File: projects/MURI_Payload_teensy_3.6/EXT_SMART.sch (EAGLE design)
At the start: 5 parts, among them U1 XBEE

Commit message: Fixed my stupid shit.
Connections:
- net VDD renamed 5V
- net PWM: now also U$1.D4
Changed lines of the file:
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@@
 <wire x1="147.32" y1="25.4" x2="182.88" y2="25.4" width="0.1524" layer="91"/>
 <wire x1="182.88" y1="25.4" x2="182.88" y2="50.8" width="0.1524" layer="91"/>
+<label x="43.18" y="25.4" size="1.778" layer="95"/>
 </segment>
 </net>
-<net name="VDD" class="0">
+<net name="5V" class="0">
 <segment>
 <label x="147.32" y="63.5" size="1.778" layer="95"/>
@@
 <wire x1="180.34" y1="53.34" x2="180.34" y2="83.82" width="0.1524" layer="91"/>
 <wire x1="180.34" y1="83.82" x2="147.32" y2="83.82" width="0.1524" layer="91"/>
+<label x="43.18" y="83.82" size="1.778" layer="95"/>
 </segment>
 </net>
@@
 <label x="175.26" y="55.88" size="1.778" layer="95" rot="MR0" xref="yes"/>
 </segment>
+<segment>
+<pinref part="U$1" gate="G$1" pin="D4"/>
+<wire x1="45.72" y1="53.34" x2="48.26" y2="53.34" width="0.1524" layer="91"/>
+<label x="48.26" y="53.34" size="1.778" layer="95" xref="yes"/>
+</segment>
 </net>

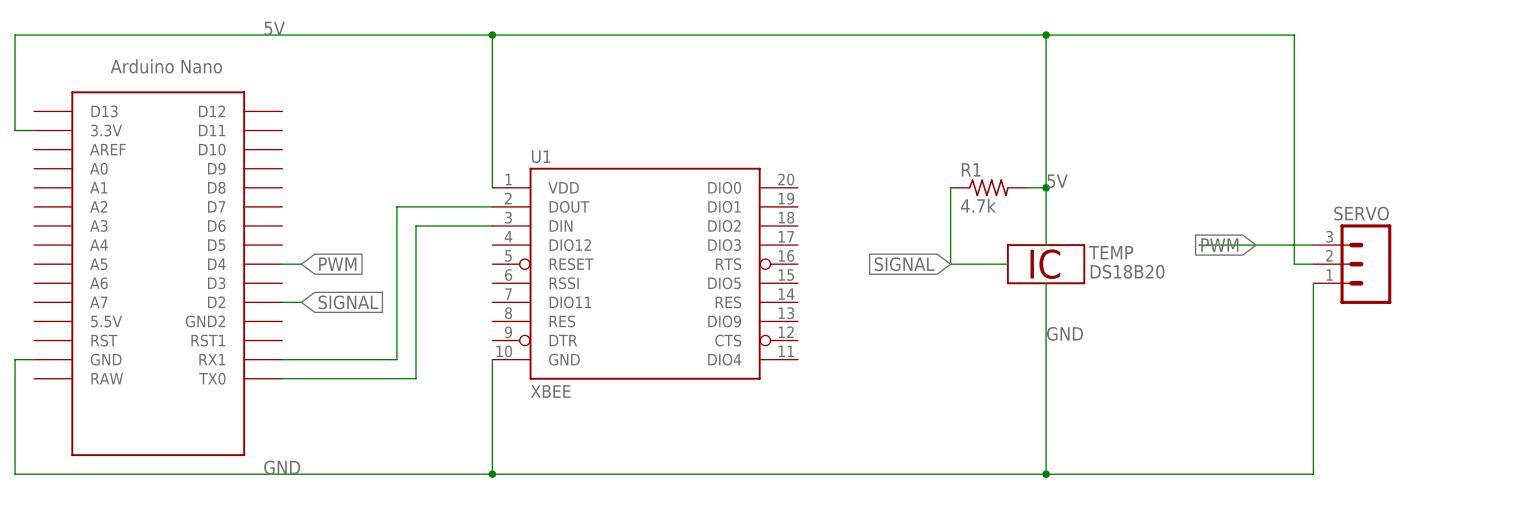
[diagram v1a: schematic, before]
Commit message: Added pin connections for XBee.
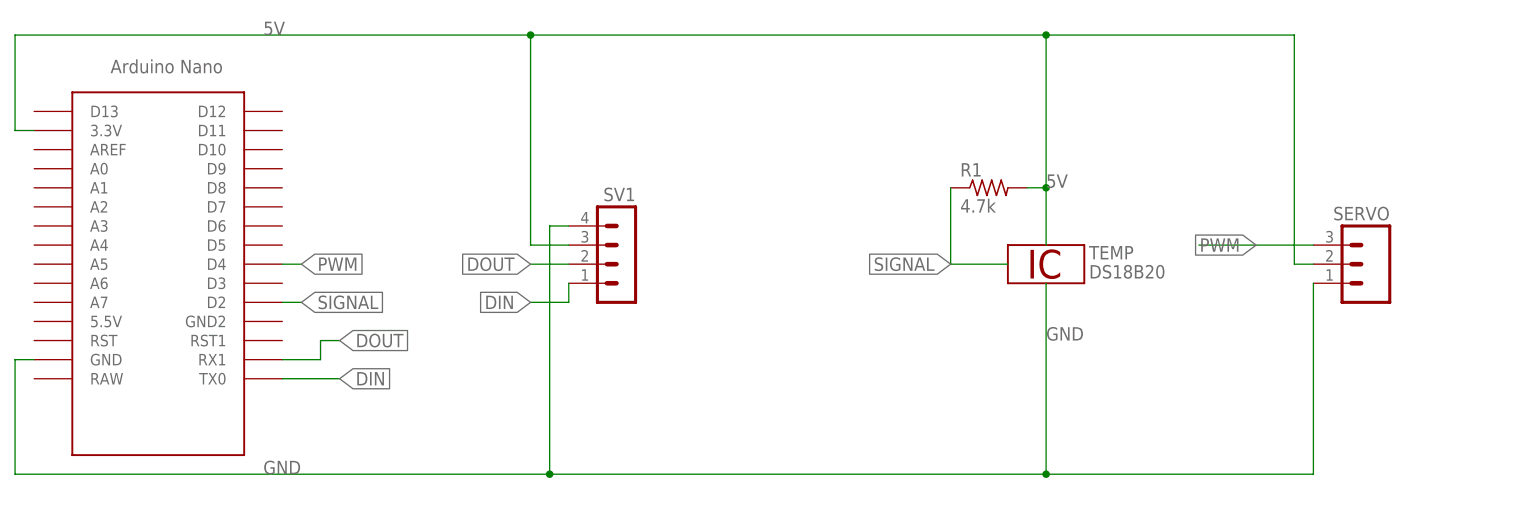
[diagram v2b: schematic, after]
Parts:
- removed U1: XBEE, SparkFun:XBEE-1B1
- added SV1: (no value), con-lstb:MA04-1
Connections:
- removed net N$3: U$1.RX1, U1.DOUT
- removed net N$4: U$1.TX0, U1.DIN
- new net DIN: SV1.1, U$1.TX0
- new net DOUT: SV1.2, U$1.RX1
- net 5V: now also SV1.3; no longer U1.VDD
- net GND: now also SV1.4; no longer U1.GND
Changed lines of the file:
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@@
 <parts>
 <part name="U$1" library="Arduino-clone" deviceset="NANO" device=""/>
-<part name="U1" library="SparkFun" deviceset="XBEE-1" device="B1" value="XBEE"/>
 <part name="TEMP" library="1wire" deviceset="DS18B20" device=""/>
 <part name="R1" library="resistor" library_urn="urn:adsk.eagle:library:348" deviceset="R-US_" device="0204/7" package3d_urn="urn:adsk.eagle:package:25945/1" value="4.7k"/>
 <part name="SERVO" library="con-amp-quick" library_urn="urn:adsk.eagle:library:125" deviceset="M03" device="" package3d_urn="urn:adsk.eagle:package:5957/1"/>
+<part name="SV1" library="con-lstb" library_urn="urn:adsk.eagle:library:162" deviceset="MA04-1" device="" package3d_urn="urn:adsk.eagle:package:8337/1"/>
 </parts>
 <sheets>
@@
 <instances>
 <instance part="U$1" gate="G$1" x="35.56" y="58.42" smashed="yes"/>
-<instance part="U1" gate="G$1" x="93.98" y="53.34" smashed="yes">
-<attribute name="NAME" x="78.74" y="66.802" size="1.6764" layer="95"/>
-<attribute name="VALUE" x="78.74" y="35.56" size="1.6764" layer="96"/>
-</instance>
 <instance part="TEMP" gate="A" x="147.32" y="53.34" smashed="yes">
 <attribute name="NAME" x="153.035" y="53.975" size="1.778" layer="95"/>
@@
 <attribute name="NAME" x="193.04" y="59.182" size="1.778" layer="95" rot="MR0"/>
 </instance>
+<instance part="SV1" gate="1" x="91.44" y="55.88" smashed="yes" rot="MR0">
+<attribute name="VALUE" x="92.71" y="45.72" size="1.778" layer="96" rot="MR0"/>
+<attribute name="NAME" x="92.71" y="61.722" size="1.778" layer="95" rot="MR0"/>
+</instance>
 </instances>
 <busses>
 </busses>
 <nets>
-<net name="N$3" class="0">
-<segment>
-<pinref part="U1" gate="G$1" pin="DOUT"/>
-<wire x1="73.66" y1="60.96" x2="60.96" y2="60.96" width="0.1524" layer="91"/>
-<wire x1="60.96" y1="60.96" x2="60.96" y2="40.64" width="0.1524" layer="91"/>
-<pinref part="U$1" gate="G$1" pin="RX1"/>
-<wire x1="60.96" y1="40.64" x2="45.72" y2="40.64" width="0.1524" layer="91"/>
-</segment>
-</net>
-<net name="N$4" class="0">
-<segment>
-<pinref part="U$1" gate="G$1" pin="TX0"/>
-<wire x1="45.72" y1="38.1" x2="63.5" y2="38.1" width="0.1524" layer="91"/>
-<wire x1="63.5" y1="38.1" x2="63.5" y2="58.42" width="0.1524" layer="91"/>
-<pinref part="U1" gate="G$1" pin="DIN"/>
-<wire x1="63.5" y1="58.42" x2="73.66" y2="58.42" width="0.1524" layer="91"/>
-</segment>
-</net>
 <net name="GND" class="0">
 <segment>
@@
 <wire x1="12.7" y1="40.64" x2="10.16" y2="40.64" width="0.1524" layer="91"/>
 <wire x1="10.16" y1="40.64" x2="10.16" y2="25.4" width="0.1524" layer="91"/>
-<wire x1="10.16" y1="25.4" x2="73.66" y2="25.4" width="0.1524" layer="91"/>
-<pinref part="U1" gate="G$1" pin="GND"/>
-<wire x1="73.66" y1="25.4" x2="147.32" y2="25.4" width="0.1524" layer="91"/>
-<wire x1="73.66" y1="40.64" x2="73.66" y2="25.4" width="0.1524" layer="91"/>
-<junction x="73.66" y="25.4"/>
+<wire x1="10.16" y1="25.4" x2="81.28" y2="25.4" width="0.1524" layer="91"/>
+<wire x1="81.28" y1="25.4" x2="147.32" y2="25.4" width="0.1524" layer="91"/>
 <wire x1="147.32" y1="50.8" x2="147.32" y2="25.4" width="0.1524" layer="91"/>
 <junction x="147.32" y="25.4"/>
@@
 <wire x1="182.88" y1="25.4" x2="182.88" y2="50.8" width="0.1524" layer="91"/>
 <label x="43.18" y="25.4" size="1.778" layer="95"/>
+<pinref part="SV1" gate="1" pin="4"/>
+<wire x1="83.82" y1="58.42" x2="81.28" y2="58.42" width="0.1524" layer="91"/>
+<wire x1="81.28" y1="58.42" x2="81.28" y2="25.4" width="0.1524" layer="91"/>
+<junction x="81.28" y="25.4"/>
 </segment>
 </net>
 <net name="5V" class="0">
 <segment>
-<label x="147.32" y="63.5" size="1.778" layer="95"/>
 <pinref part="U$1" gate="G$1" pin="3.3V"/>
 <wire x1="12.7" y1="71.12" x2="10.16" y2="71.12" width="0.1524" layer="91"/>
 <wire x1="10.16" y1="71.12" x2="10.16" y2="83.82" width="0.1524" layer="91"/>
-<wire x1="10.16" y1="83.82" x2="73.66" y2="83.82" width="0.1524" layer="91"/>
-<pinref part="U1" gate="G$1" pin="VDD"/>
-<wire x1="73.66" y1="83.82" x2="147.32" y2="83.82" width="0.1524" layer="91"/>
-<wire x1="73.66" y1="63.5" x2="73.66" y2="83.82" width="0.1524" layer="91"/>
-<junction x="73.66" y="83.82"/>
-<wire x1="147.32" y1="83.82" x2="147.32" y2="63.5" width="0.1524" layer="91"/>
-<junction x="147.32" y="83.82"/>
-<pinref part="R1" gate="G$1" pin="2"/>
-<wire x1="147.32" y1="63.5" x2="147.32" y2="55.88" width="0.1524" layer="91"/>
-<wire x1="144.78" y1="63.5" x2="147.32" y2="63.5" width="0.1524" layer="91"/>
-<junction x="147.32" y="63.5"/>
+<wire x1="10.16" y1="83.82" x2="78.74" y2="83.82" width="0.1524" layer="91"/>
+<wire x1="78.74" y1="83.82" x2="147.32" y2="83.82" width="0.1524" layer="91"/>
+<wire x1="147.32" y1="83.82" x2="180.34" y2="83.82" width="0.1524" layer="91"/>
 <pinref part="SERVO" gate="G$1" pin="2"/>
 <wire x1="182.88" y1="53.34" x2="180.34" y2="53.34" width="0.1524" layer="91"/>
 <wire x1="180.34" y1="53.34" x2="180.34" y2="83.82" width="0.1524" layer="91"/>
-<wire x1="180.34" y1="83.82" x2="147.32" y2="83.82" width="0.1524" layer="91"/>
 <label x="43.18" y="83.82" size="1.778" layer="95"/>
+<pinref part="R1" gate="G$1" pin="2"/>
+<wire x1="144.78" y1="63.5" x2="147.32" y2="63.5" width="0.1524" layer="91"/>
+<wire x1="147.32" y1="63.5" x2="147.32" y2="55.88" width="0.1524" layer="91"/>
+<label x="147.32" y="63.5" size="1.778" layer="95"/>
+<wire x1="147.32" y1="63.5" x2="147.32" y2="83.82" width="0.1524" layer="91"/>
+<junction x="147.32" y="63.5"/>
+<junction x="147.32" y="83.82"/>
+<pinref part="SV1" gate="1" pin="3"/>
+<wire x1="83.82" y1="55.88" x2="78.74" y2="55.88" width="0.1524" layer="91"/>
+<wire x1="78.74" y1="55.88" x2="78.74" y2="83.82" width="0.1524" layer="91"/>
+<junction x="78.74" y="83.82"/>
 </segment>
 </net>
@@
 </segment>
 </net>
+<net name="DOUT" class="0">
+<segment>
+<pinref part="SV1" gate="1" pin="2"/>
+<wire x1="83.82" y1="53.34" x2="78.74" y2="53.34" width="0.1524" layer="91"/>
+<label x="78.74" y="53.34" size="1.778" layer="95" rot="MR0" xref="yes"/>
+</segment>
+<segment>
+<pinref part="U$1" gate="G$1" pin="RX1"/>
+<wire x1="45.72" y1="40.64" x2="50.8" y2="40.64" width="0.1524" layer="91"/>
+<wire x1="50.8" y1="40.64" x2="50.8" y2="43.18" width="0.1524" layer="91"/>
+<wire x1="50.8" y1="43.18" x2="53.34" y2="43.18" width="0.1524" layer="91"/>
+<label x="53.34" y="43.18" size="1.778" layer="95" xref="yes"/>
+</segment>
+</net>
+<net name="DIN" class="0">
+<segment>
+<pinref part="SV1" gate="1" pin="1"/>
+<wire x1="83.82" y1="50.8" x2="83.82" y2="48.26" width="0.1524" layer="91"/>
+<wire x1="83.82" y1="48.26" x2="78.74" y2="48.26" width="0.1524" layer="91"/>
+<label x="78.74" y="48.26" size="1.778" layer="95" rot="MR0" xref="yes"/>
+</segment>
+<segment>
+<pinref part="U$1" gate="G$1" pin="TX0"/>
+<wire x1="45.72" y1="38.1" x2="53.34" y2="38.1" width="0.1524" layer="91"/>
+<label x="53.34" y="38.1" size="1.778" layer="95" xref="yes"/>
+</segment>
+</net>

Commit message: I'm an idiot.
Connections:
- net 5V: now also U$1.5.5V; no longer U$1.3.3V
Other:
- moved on the sheet: R1, SERVO, SV1, TEMP

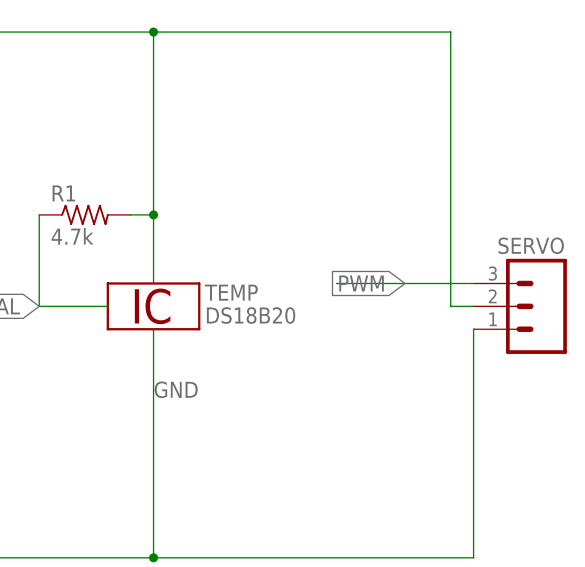
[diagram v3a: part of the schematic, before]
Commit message: Fixed wiring of MS5607 and updated external SMART schematic.
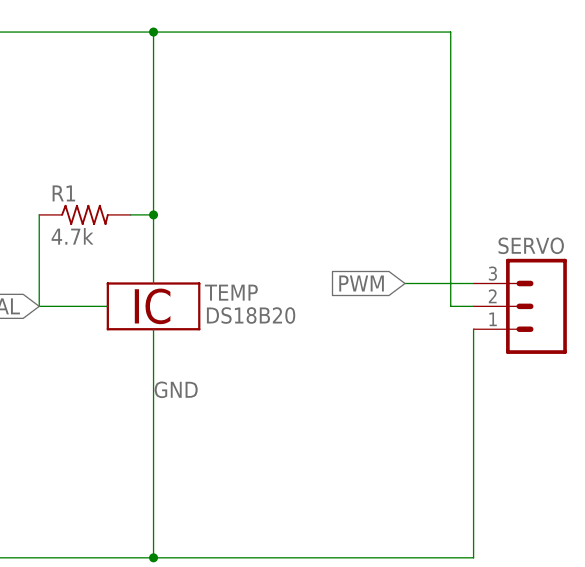
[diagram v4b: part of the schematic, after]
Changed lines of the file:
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@@
 <segment>
 <pinref part="SERVO" gate="G$1" pin="3"/>
-<wire x1="200.66" y1="53.34" x2="185.42" y2="53.34" width="0.1524" layer="91"/>
+<wire x1="200.66" y1="53.34" x2="193.04" y2="53.34" width="0.1524" layer="91"/>
 <label x="193.04" y="53.34" size="1.778" layer="95" rot="MR0" xref="yes"/>
 </segment>
